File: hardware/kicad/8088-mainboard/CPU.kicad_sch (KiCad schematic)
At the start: 14 parts, among them U1 8088, U3 74LS373, U4 74LS373, U5 74LS245, U6 8288

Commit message: Add PSB board design
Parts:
- removed R5, R6, R7, R8: 10k, Resistor_THT:R_Axial_DIN0207_L6.3mm_D2.5mm_P7.62mm_Horizontal, symbol Device:R
- added J_DEBUG1: DEBUG, Connector_PinHeader_2.54mm:PinHeader_1x10_P2.54mm_Vertical, symbol Connector_Generic:Conn_01x10
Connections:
- net ALE: now also J_DEBUG1.5 (Pin_5)
- net CLK: now also J_DEBUG1.2 (Pin_2)
- net DEN: now also J_DEBUG1.10 (Pin_10)
- net GND: now also U1.17 (NMI), U1.18 (INTR), U1.23 (~{TEST}), U1.31 (HOLD), J_DEBUG1.1 (Pin_1)
- net IORC: now also J_DEBUG1.8 (Pin_8)
- net IOWC: now also J_DEBUG1.9 (Pin_9)
- net MRDC: now also J_DEBUG1.6 (Pin_6)
- net MWTC: now also J_DEBUG1.7 (Pin_7)
- net READY: now also J_DEBUG1.4 (Pin_4)
- net RESET: now also J_DEBUG1.3 (Pin_3)

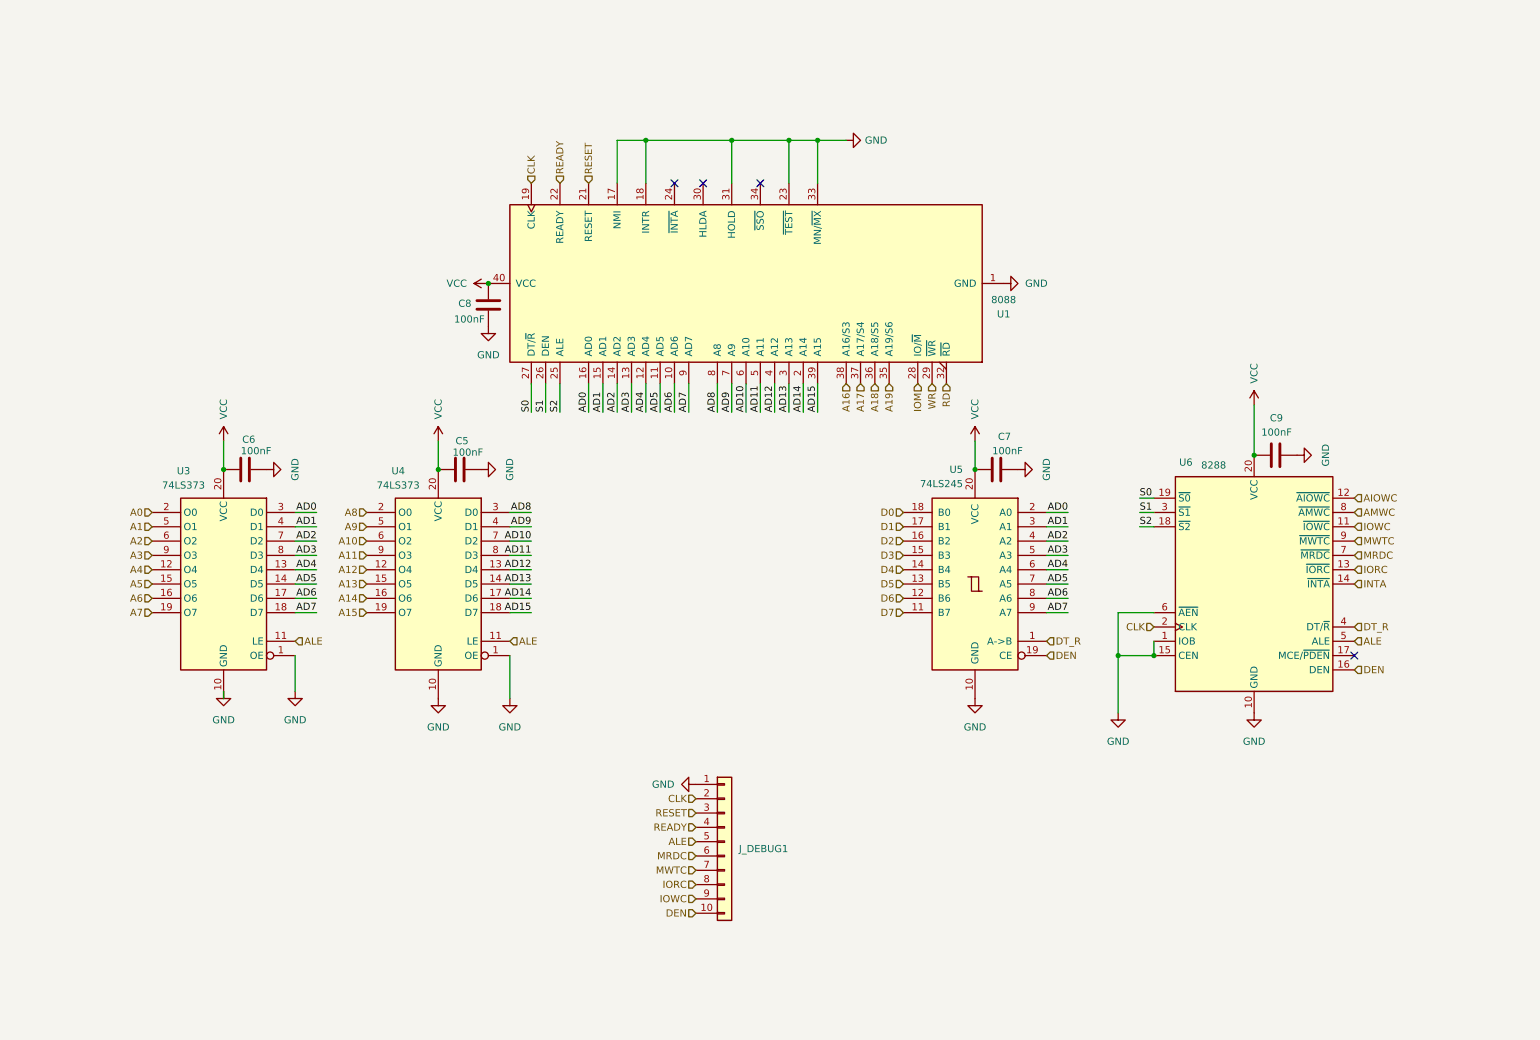
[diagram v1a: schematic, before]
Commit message: Update 8088-mainboard schematics for refined connections and label adjustments
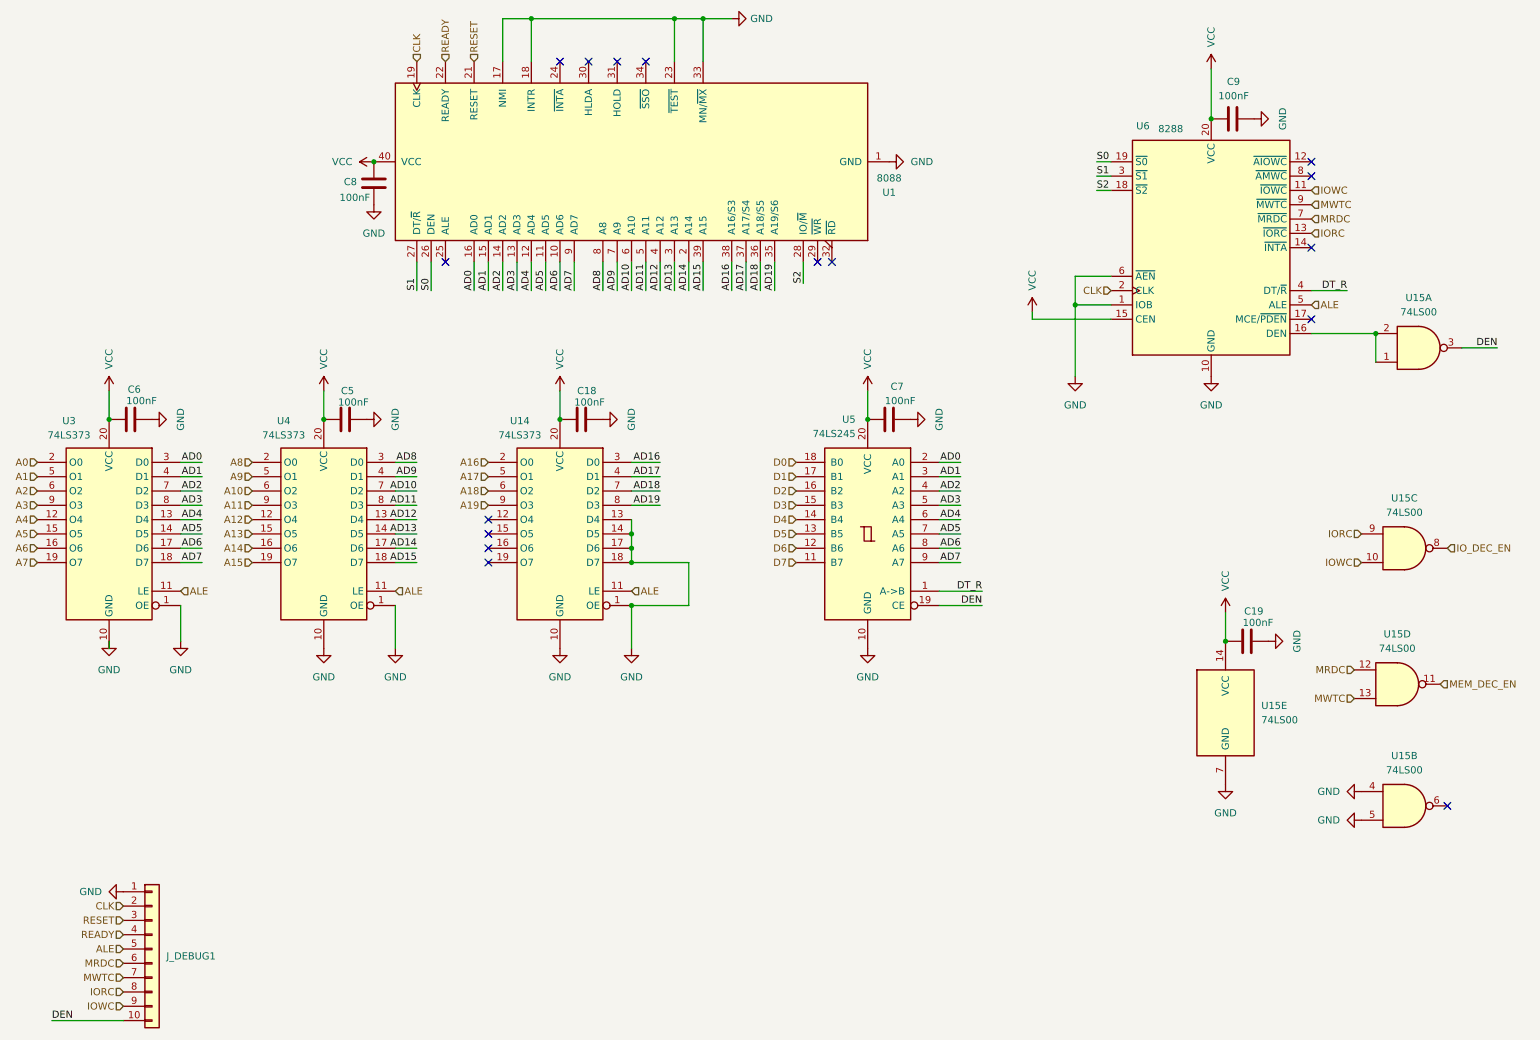
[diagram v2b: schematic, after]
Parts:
- added C18, C19: 100nF, Capacitor_THT:C_Disc_D5.0mm_W2.5mm_P5.00mm, symbol Device:C
- added U14: 74LS373, Package_DIP:DIP-20_W7.62mm, symbol 74xx:74LS373
- added U15: 74LS00, Package_DIP:DIP-14_W7.62mm, symbol 74xx:74LS00
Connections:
- net IOM is gone; now on net S2: U1.28 (IO/~{M})
- net A16: now also U14.2 (O0); no longer U1.38 (A16/S3)
- net A17: now also U14.5 (O1); no longer U1.37 (A17/S4)
- net A18: now also U14.6 (O2); no longer U1.36 (A18/S5)
- net A19: now also U14.9 (O3); no longer U1.35 (A19/S6)
- net ALE: now also U14.11 (LE)
- net DEN: now also U15.3; no longer U6.16 (DEN)
- net GND: now also C18.2, C19.2, U14.1 (OE), U14.10 (GND), U14.13 (D4), U14.14 (D5), U14.17 (D6), U14.18 (D7), U15.4, U15.5, U15.7 (GND); no longer U1.31 (HOLD), U6.15 (CEN)
- net IORC: now also U15.9
- net IOWC: now also U15.10
- net MRDC: now also U15.12
- net MWTC: now also U15.13
- net S0: now also U1.26 (DEN); no longer U1.27 (DT/~{R})
- net S1: now also U1.27 (DT/~{R}); no longer U1.26 (DEN)
- net S2: no longer U1.25 (ALE)
- net VCC: now also U6.15 (CEN), C18.1, C19.1, U14.20 (VCC), U15.14 (VCC)
- net AIOWC: no longer names the net of U6.12 (~{AIOWC})
- net AMWC: no longer names the net of U6.8 (~{AMWC})
- net INTA: no longer names the net of U6.14 (~{INTA})
- net RD: no longer names the net of U1.32 (~{RD})
- net WR: no longer names the net of U1.29 (~{WR})
- new net: U15.1, U15.2, U6.16 (DEN)
- new net AD16: U1.38 (A16/S3), U14.3 (D0)
- new net AD17: U1.37 (A17/S4), U14.4 (D1)
- new net AD18: U1.36 (A18/S5), U14.7 (D2)
- new net AD19: U1.35 (A19/S6), U14.8 (D3)
- new net IO_DEC_EN: U15.8
- new net MEM_DEC_EN: U15.11
- no-connect marks 4 -> 16
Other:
- moved on the sheet: C5, C6, C7, C8, C9, J_DEBUG1, U1, U3, U4, U5, U6

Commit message: Update 8086-mainboard scheme
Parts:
- removed C5: 100nF, Capacitor_THT:C_Disc_D5.0mm_W2.5mm_P5.00mm, symbol Device:C
- removed U1: 8088, Package_DIP:DIP-40_W15.24mm, symbol MCU_Intel:8088
- removed U4: 74LS373, Package_DIP:DIP-20_W7.62mm, symbol 74xx:74LS373
- added U1: 8088_Max_Mode, Package_DIP:DIP-40_W15.24mm, symbol MCU_Intel:8088_Max_Mode
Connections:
- net A10: now also U1.6 (A10)
- net A11: now also U1.5 (A11)
- net A12: now also U1.4 (A12)
- net A13: now also U1.3 (A13)
- net A14: now also U1.2 (A14)
- net A15: now also U1.39 (A15)
- net A8: now also U1.8 (A8)
- net A9: now also U1.7 (A9)
- net AD0: now also U1.16 (AD0)
- net AD1: now also U1.15 (AD1)
- net AD16: now also U1.38 (A16/S3)
- net AD17: now also U1.37 (A17/S4)
- net AD18: now also U1.36 (A18/S5)
- net AD19: now also U1.35 (A19/S6)
- net AD2: now also U1.14 (AD2)
- net AD3: now also U1.13 (AD3)
- net AD4: now also U1.12 (AD4)
- net AD5: now also U1.11 (AD5)
- net AD6: now also U1.10 (AD6)
- net AD7: now also U1.9 (AD7)
- net CLK: now also U1.19 (CLK)
- net DEN: now also U15.8; no longer U15.3
- net GND: now also U15.12, U15.13, U1.1 (GND), U1.17 (NMI), U1.18 (INTR), U1.20 (GND), U1.23 (~{TEST}), U1.33 (MN/~{MX}); no longer U15.4, U15.5
- net IORC: now also U15.2; no longer U15.9
- net IOWC: now also U15.1; no longer U15.10
- net IO_DEC_EN: now also U15.3; no longer U15.8
- net MEM_DEC_EN: now also U15.6; no longer U15.11
- net MRDC: now also U15.4; no longer U15.12
- net MWTC: now also U15.5; no longer U15.13
- net READY: now also U1.22 (READY)
- net RESET: now also U1.21 (RESET)
- net S0: now also U1.26 (~{S0})
- net S1: now also U1.27 (~{S1})
- net S2: now also U1.28 (~{S2})
- net VCC: now also U1.40 (VCC)
- new net: U15.10, U15.9, U6.16 (DEN)
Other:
- moved on the sheet: C18, C19, C6, C7, U14, U15A, U15B, U15C, U15D, U15E, U3, U5

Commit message: Update 8088-mainboard schematics
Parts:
- removed C19, C9: 100nF, Capacitor_THT:C_Disc_D5.0mm_W2.5mm_P5.00mm, symbol Device:C
- removed U1: 8088_Max_Mode, Package_DIP:DIP-40_W15.24mm, symbol MCU_Intel:8088_Max_Mode
- removed U15: 74LS00, Package_DIP:DIP-14_W7.62mm, symbol 74xx:74LS00
- removed U6: 8288, Package_DIP:DIP-20_W7.62mm, symbol Interface:8288
- added U1: 8088_Min_Mode, Package_DIP:DIP-40_W15.24mm, symbol MCU_Intel:8088_Min_Mode
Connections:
- net IOWC is gone; now on net DT_R: J_DEBUG1.9 (Pin_9)
- net A10: now also U1.6 (A10)
- net A11: now also U1.5 (A11)
- net A12: now also U1.4 (A12)
- net A13: now also U1.3 (A13)
- net A14: now also U1.2 (A14)
- net A15: now also U1.39 (A15)
- net A8: now also U1.8 (A8)
- net A9: now also U1.7 (A9)
- net AD0: now also U1.16 (AD0)
- net AD1: now also U1.15 (AD1)
- net AD16: now also U1.38 (A16/S3)
- net AD17: now also U1.37 (A17/S4)
- net AD18: now also U1.36 (A18/S5)
- net AD19: now also U1.35 (A19/S6)
- net AD2: now also U1.14 (AD2)
- net AD3: now also U1.13 (AD3)
- net AD4: now also U1.12 (AD4)
- net AD5: now also U1.11 (AD5)
- net AD6: now also U1.10 (AD6)
- net AD7: now also U1.9 (AD7)
- net ALE: now also U1.25 (ALE)
- net CLK: now also U1.19 (CLK)
- net DEN: now also U1.26 (DEN)
- net DT_R: now also U1.27 (DT/~{R})
- net GND: now also U1.1 (GND), U1.17 (NMI), U1.18 (INTR), U1.20 (GND), U1.23 (~{TEST}), U1.31 (HOLD)
- net READY: now also U1.22 (READY)
- net RESET: now also U1.21 (RESET)
- net VCC: now also U1.33 (MN/~{MX}), U1.40 (VCC)
- net IORC renamed RD
- net RD: now also U1.32 (~{RD})
- net MRDC renamed IOM
- net IOM: now also U1.28 (IO/~{M})
- net MWTC renamed WR
- net WR: now also U1.29 (~{WR})
- no-connect marks 16 -> 7
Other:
- moved on the sheet: C8

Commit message: Finalize 8088 mainboard rev1.0 for production
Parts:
- J1: renamed from J_DEBUG1; value DEBUG -> Conn_01x10
- U1: footprint Package_DIP:DIP-40_W15.24mm -> Package_DIP:DIP-40_W15.24mm_Socket
- U2: renamed from U3; footprint Package_DIP:DIP-20_W7.62mm -> Package_DIP:DIP-20_W7.62mm_Socket
- U3: renamed from U14; footprint Package_DIP:DIP-20_W7.62mm -> Package_DIP:DIP-20_W7.62mm_Socket
- U4: renamed from U5; footprint Package_DIP:DIP-20_W7.62mm -> Package_DIP:DIP-20_W7.62mm_Socket
- renumbered C8 to C1, C6 to C2, C18 to C3, C7 to C4
